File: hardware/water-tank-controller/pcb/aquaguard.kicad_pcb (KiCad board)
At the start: 2 copper layers, 109.3 x 83.2 mm, 40 parts, among them J1 2P 5.08mm, J2 2P 5.08mm, J3 4P 3.5mm, J4 3P 3.5mm, J5 3P 2.54mm, K1 SRD-05VDC-SL-C, Q1 S8050, SW1 Tactile 6mm, SW2 Tactile 6mm, U1 ESP32-WROOM-32E (4MB), U2 AMS1117-3.3, U3 PC817

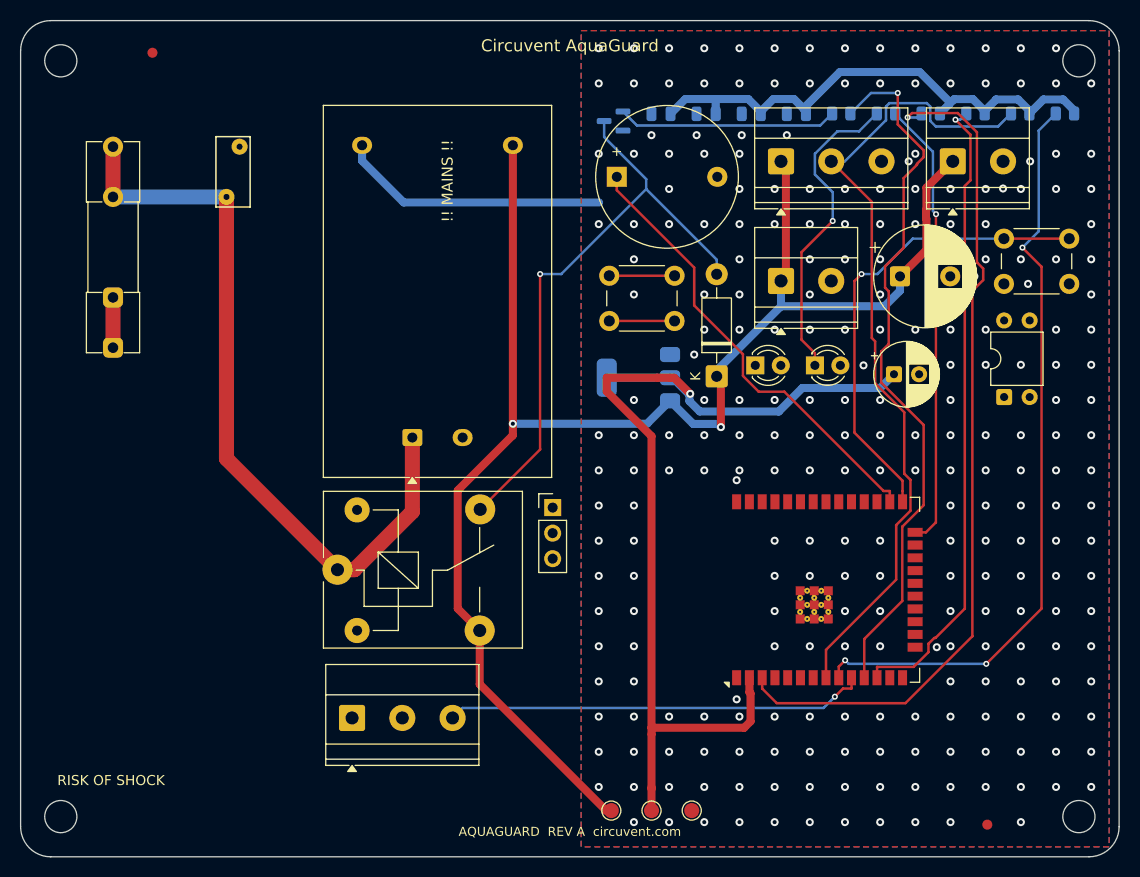
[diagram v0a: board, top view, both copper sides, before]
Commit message: hardware: fix mains isolation barrier gaps, add load-controller PCB
Adds the 13th board (ultra-compact dual-channel load controller: ESP32-C3,
opto+relay channel, MOSFET PWM channel, USB-C, AP2112K LDO, USBLC6 ESD) and
regenerates all 12 existing boards, which were stale with respect to earlier
relay-pinout and LED-polarity fixes.

The substantive change is to the mains isolation barrier. It is a keepout band
the router must not cross, deliberately cut where a component straddles it
because there the isolation is provided by the part's package. Three linked
defects made those cuts unsafe, each only visible once the previous was fixed:

1. The cut removed the barrier across the full band width for the straddling
   part's whole height, while the ISO_BRIDGE area that excuses the gap covered
   only the part itself. The router used the leftover strip beside the part to
   bring +5V within 6.99 mm of AC_N against an 8.0 mm reinforced creepage rule.
2. Straddling parts can overlap in y, so cutting per part put one part's
   keepout on another part's pads. The exempt x-ranges are now unioned per
   strip by a sweep line.
3. The rule only relaxes for items insideArea('ISO_BRIDGE'). With the hole the
   same size as the area, a track could hug the hole's edge without being
   contained in it, so the rule fired anyway and the router had no way to know.
   The hole is now the part's pad bbox + 0.3 mm, strictly inside ISO_BRIDGE at
   the footprint bbox + 0.6 mm.

The tighter hole leaves mains nets less room to reach bridge pads, so some
boards report more unconnected items. That is deliberate: those are documented
hand-routing items, whereas a creepage violation is a safety defect.

Also fixed in the generator:
- _pad_shape() derived a pad's layers from PAD::GetLayer(), which returns F.Cu
  even for pads on B.Cu. Every back-side pad became a phantom obstacle on the
  front, blocking legal paths there while hiding the real one behind. Only
  IsOnLayer() is truthful.
- Castella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
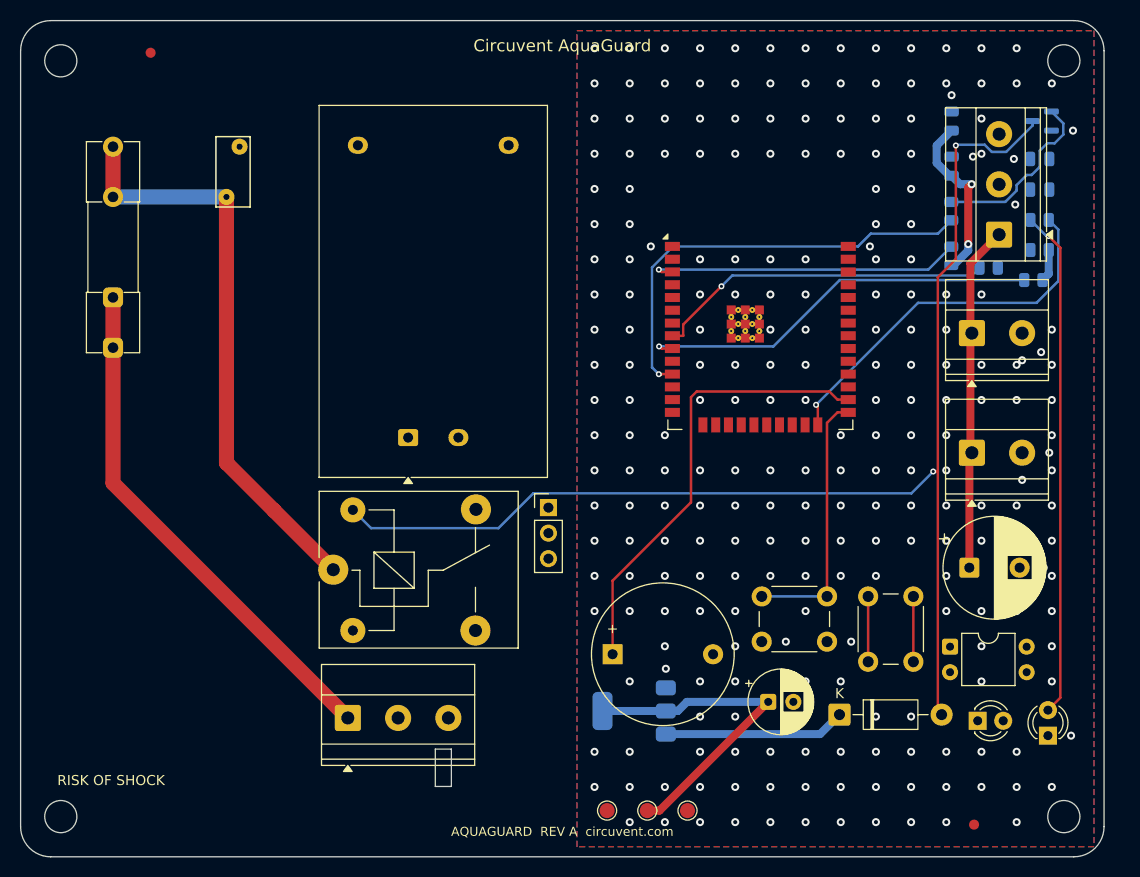
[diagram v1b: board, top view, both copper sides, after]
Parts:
- moved FB1 47.5 mm to (158.9, 143.0)
- moved SW2 46.2 mm to (184.3, 143.8), turned to 90 degrees
- moved LED2 43.5 mm to (202.2, 151.1), turned to 90 degrees
- moved SW1 43.0 mm to (173.7, 137.3)
- moved Q1 42.6 mm to (201.6, 90.0)
- moved LED1 41.7 mm to (195.2, 149.7)
- moved D1 35.8 mm to (181.5, 149.1), turned to 0 degrees
- moved C2 34.9 mm to (174.4, 147.8)
- moved U2 33.2 mm to (161.0, 148.7)
- moved C1 29.8 mm to (194.4, 134.4)
- moved C5 29.1 mm to (201.4, 93.8)
- moved U1 29.0 mm to (173.6, 107.7), turned to 0 degrees
- moved C3 28.9 mm to (192.6, 90.0), turned to 90 degrees
- moved J3 25.5 mm to (194.6, 123.0)
- moved U3 25.4 mm to (192.5, 142.3), turned to 0 degrees
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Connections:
- K1 pad 2: MOTOR_RELAY_SW -> +5V
- K1 pad 3: +5V -> MOTOR_RELAY_SW
- K1 pad 4: MOTOR_RELAY_COIL -> N$K1.4
- K1 pad 5: N$K1.5 -> MOTOR_RELAY_COIL
- LED2 pad 1: LED_PIN_A -> GND
- LED2 pad 2: GND -> LED_PIN_A
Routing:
- net +5V: track 155.1 -> 52.8 mm, vias 2 -> 0
- net +3V3: track 152.6 -> 53.8 mm, vias 1 -> 2
- net MOTOR_RELAY_COIL: track 59.8 -> 128.3 mm, vias 1 -> 2
- net US_ECHO: track 63.5 -> 0.00 mm, vias 1 -> 0
- net EN: track 85.6 -> 31.5 mm
- net FLOAT_LOW: track 81.5 -> 34.0 mm, vias 0 -> 1
- net AC_L: track 5.00 -> 51.5 mm
- net US_TRIG: track 42.0 -> 0.00 mm, vias 1 -> 0
- net FLOAT_HIGH: track 75.4 -> 40.5 mm, vias 3 -> 1
- net MOTOR_RELAY: track 71.0 -> 44.0 mm
- net GND: track 26.8 -> 0.00 mm, vias 261 -> 246
- net BTN_PIN: track 47.1 -> 26.3 mm, vias 1 -> 0
- net LED_PIN_A: track 31.5 -> 50.6 mm
- net AC_L_FUSED: track 75.2 -> 57.8 mm
- net LED_PIN: track 44.8 -> 37.8 mm
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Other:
- board size 109.3 x 83.2 mm -> 107.8 x 83.2 mm
- board text removed: "!! MAINS !!"

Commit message: Release 1.10.0, and stop shipping permissions the app never uses
Cut 1.10.0 (versionCode 12) and built it: AAB 38 MB, APK 83 MB, signed with the
upload key, JS bundle embedded.

Checking the generated manifest before writing the Play listing turned up
permissions no one had asked for. Every one of them is printed on the store page
for users to read before they install:

  RECORD_AUDIO          expo-camera asks for the microphone so video can be
                        recorded with sound. This app only ever puts the camera
                        in barcode mode to read a QR label, and expo-speech is
                        output-only - it speaks, it does not listen. Left in,
                        Play lists "Microphone" against a home-control app,
                        which is alarming, unexplainable and untrue.
  SYSTEM_ALERT_WINDOW   React Native's development overlay, useless in a release
                        build and shown to users as "Display over other apps".
  READ/WRITE_EXTERNAL_STORAGE
                        Legacy storage access nothing here touches.

Stripped via android.blockedPermissions. That emits tools:node="remove", which
is a merge instruction rather than a guarantee, so it was checked against the
finished artifact with aapt2 rather than the source manifest - all four are
absent from the APK.

NEARBY_WIFI_DEVICES now carries neverForLocation. Android otherwise treats it as
location-capable, because knowing which networks are in range is enough to place
someone, and Play's data safety review treats it the same way. The app uses it
only to join a new device's setup hotspot. That flag is a promise, so the plugin
says plainly that it has to come off if scan results are ever used positionally.

What is left is defensible: location for Wi-Fi onboarding (Android requires it),
camera for the QR label, nearby-devices flagged as non-positional.

Added mobile/store/listing with the text Play asks for - title, short and full
descriptions, and what'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
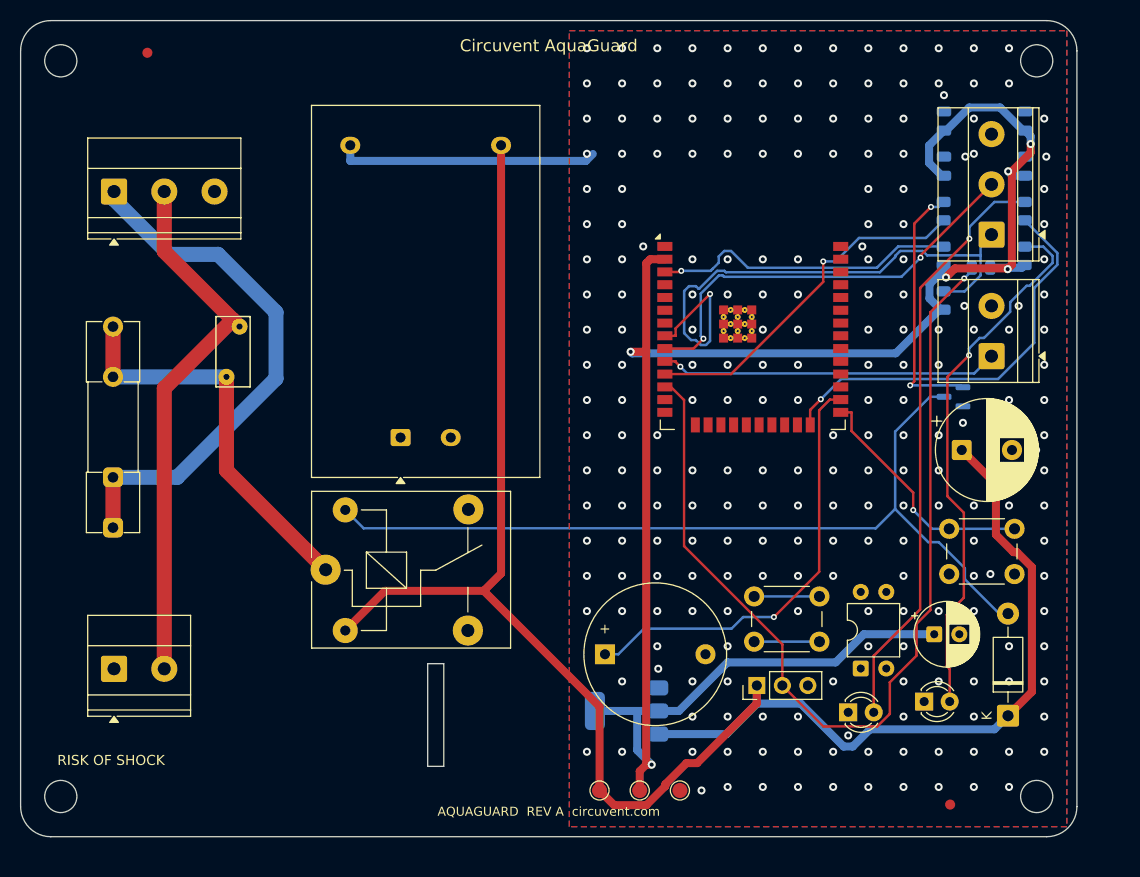
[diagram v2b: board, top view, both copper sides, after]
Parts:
- moved J2 91.7 mm to (109.3, 144.5)
- moved J1 57.3 mm to (109.3, 97.0)
- moved Q1 28.8 mm to (192.8, 117.4)
- moved J5 27.3 mm to (173.3, 146.2), turned to 90 degrees
- moved LED2 20.0 mm to (182.3, 148.8), turned to 0 degrees
- moved SW1 19.8 mm to (192.4, 130.6)
- moved F1 17.9 mm to (109.2, 130.4)
- moved RV1 17.9 mm to (120.5, 115.4)
- moved C2 17.8 mm to (190.9, 141.1)
- moved D1 16.8 mm to (198.2, 149.2), turned to 90 degrees
- moved SW2 13.1 mm to (173.0, 137.3), turned to 0 degrees
- moved C1 11.7 mm to (193.6, 122.7)
- moved J3 9.81 mm to (196.6, 113.4), turned to 90 degrees
- moved C5 9.56 mm to (191.9, 94.5), turned to 90 degrees
- moved R6 9.16 mm to (191.8, 107.9), turned to 90 degrees
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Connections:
- J1 pad 3: US_TRIG -> PE
- J2 pad 1: +5V -> MOTOR_RELAY_SW
- J2 pad 2: GND -> AC_N
- J3 pad 1: +5V -> US_TRIG
- J4 pad 1: +5V -> FLOAT_LOW
- J4 pad 2: FLOAT_LOW -> FLOAT_HIGH
- J5 pad 2: MOTOR_RELAY_SW -> US_ECHO
- J5 pad 3: AC_N -> GND
- LED1 pad 1: N$LED1.1 -> GND
- LED1 pad 2: N$LED1.2 -> LED1_A
- R4 pad 2: US_ECHO -> LED1_A
- R5 pad 2: FLOAT_LOW -> US_ECHO
- R6 pad 2: FLOAT_HIGH -> FLOAT_LOW
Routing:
- net +3V3: track 53.8 -> 182.0 mm, vias 2 -> 6
- net +5V: track 52.8 -> 178.9 mm
- net US_ECHO: track 0.00 -> 95.6 mm, vias 0 -> 1
- net AC_N: track 0.00 -> 54.1 mm
- net LED1_A: track 0.00 -> 53.8 mm, vias 0 -> 1
- net MOTOR_RELAY_COIL: track 128.3 -> 86.5 mm, vias 2 -> 0
- net US_TRIG: track 0.00 -> 33.8 mm, vias 0 -> 1
- net GND: track 0.00 -> 26.0 mm, vias 246 -> 234
- net FLOAT_LOW: track 34.0 -> 59.3 mm
- net AC_L_FUSED: track 57.8 -> 39.6 mm
- net MOTOR_RELAY: track 44.0 -> 35.3 mm
- net LED_PIN_A: track 50.6 -> 58.8 mm
- net MOTOR_RELAY_B: track 18.0 -> 25.4 mm, vias 0 -> 2
- net LED_PIN: track 37.8 -> 41.0 mm
- net BTN_PIN: track 26.3 -> 24.2 mm, vias 0 -> 1
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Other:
- board size 107.8 x 83.2 mm -> 105.1 x 81.2 mm
